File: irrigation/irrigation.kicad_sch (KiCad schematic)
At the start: 43 parts, among them J1 24V Jmp, J10 24V, J11 25%, J12 50%, J13 75%, J14 100%, J15 100%, J16 100%, J17 Pump, J18 Outlet Pump, J19 Empty, J2 Power, J3 Power, J4 Power, J5 Power, J6 Power, J7 Power, J8 0V Jmp, J9 Empty, K1 PLC-RPT-24DC/21, K2 PLC-RPT-24DC/21, K3 PLC-RPT-24DC/21, M1 Well Pump, M2 Outlet Pump, SW1 Well Empty, SW2 100% Full, SW3 25% Full, SW4 50% Full, SW5 75% Full, SW6 Drain Switch, SW7 Fill Switch, U1 MPPT-Charger

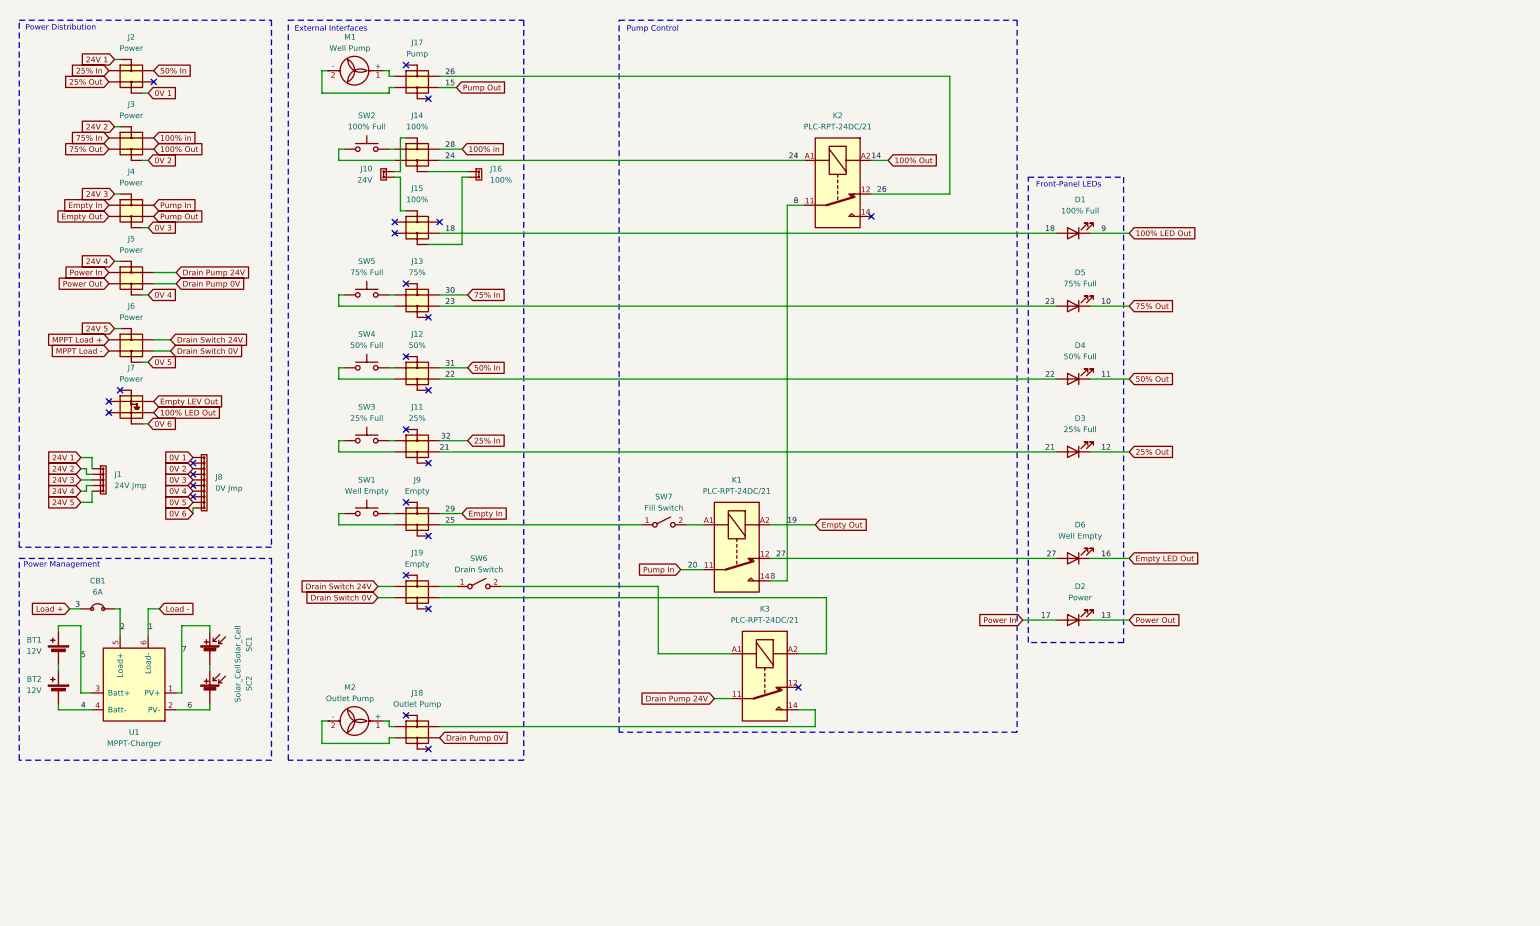
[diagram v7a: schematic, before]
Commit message: Adding another relay for outlet pump control
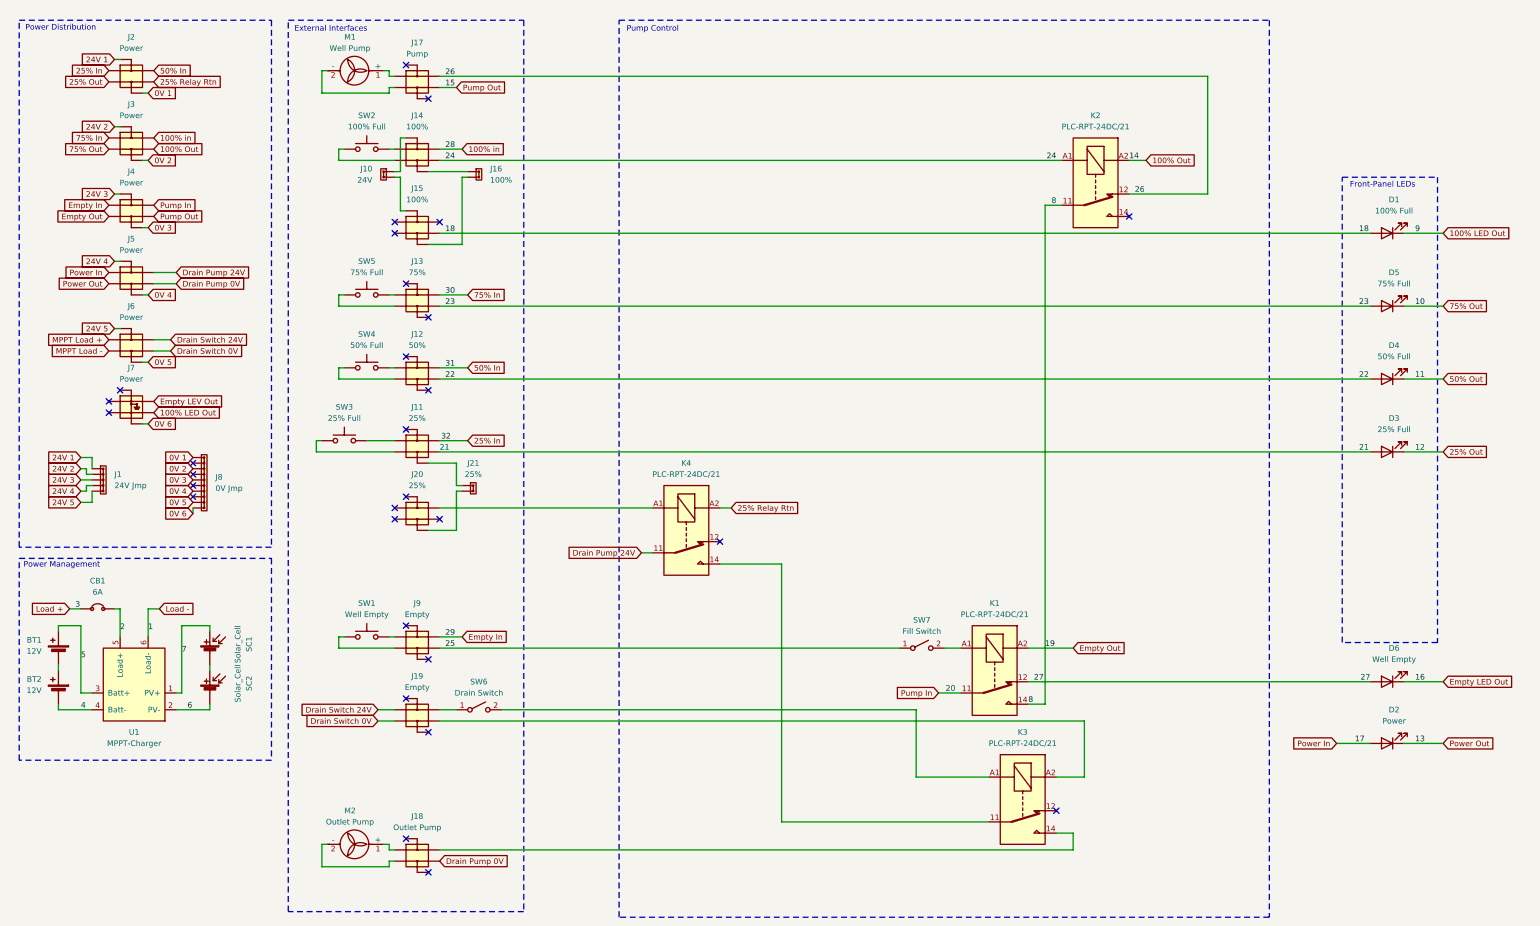
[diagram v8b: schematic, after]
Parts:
- added J20: 25%, symbol Phoenix Contact:PTTB_2,5-L/N_3210994
- added J21: 25%, symbol Phoenix Contact:FBS 2-5_3030161
- added K4: PLC-RPT-24DC/21, symbol Phoenix Contact:PLC-RPT-24DC/21
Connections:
- net Drain Pump 24V: now also K4.11; no longer K3.11
- net at J10.: now also J15.; no longer J14.
- net at J16.: now also J15.; no longer J14.
- new net: J10., J14.
- new net: J14., J16.
- new net: K3.11, K4.14
- new net: J20., J21.
- new net: J11., J21.
- new net: J20., K4.A1
- new net 25% Relay Rtn: J2., K4.A2
- no-connect marks 27 -> 30
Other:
- moved on the sheet: D1, D2, D3, D4, D5, D6, J18, J19, J9, K1, K2, K3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
